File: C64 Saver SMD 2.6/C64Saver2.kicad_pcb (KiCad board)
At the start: 2 copper layers, 43.9 x 28.8 mm, 26 parts, among them J1 Conn_01x04, J2 Conn_01x08, J4 Conn_01x08, J5 Conn_01x04, J6 Conn_01x04, Q1 2N7002, Q2 IRFR5305, U1 TL431DBZ

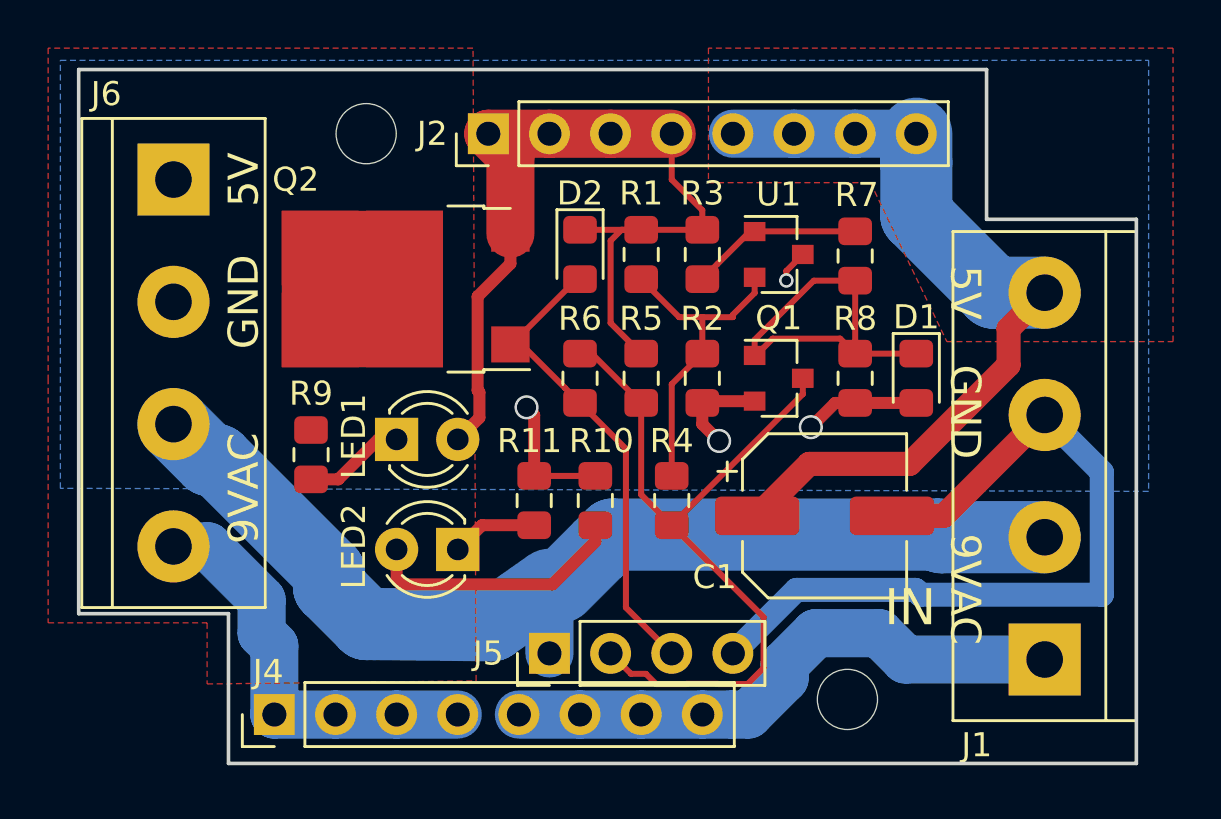
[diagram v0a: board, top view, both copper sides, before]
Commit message: SMD version 2.6 layout and schematics. Both THT and SMD are now on same version. should have same references.
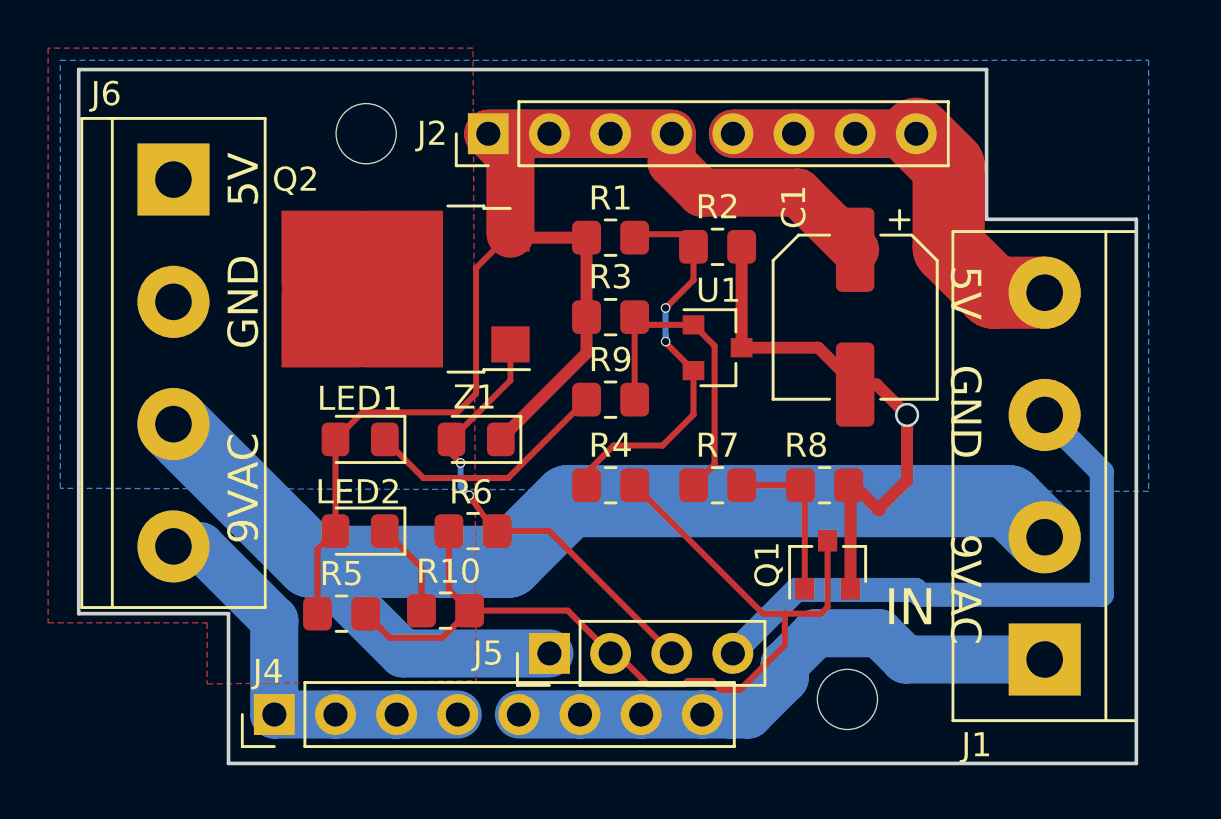
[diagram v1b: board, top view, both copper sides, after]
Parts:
- removed D1, D2: BZY55B6V8, Diode_SMD:D_0805_2012Metric_Pad1.15x1.40mm_HandSolder
- removed R11: 3k3, Resistor_SMD:R_0805_2012Metric_Pad1.15x1.40mm_HandSolder
- added Z1: BZY55B6V8, Diode_SMD:D_0805_2012Metric_Pad1.15x1.40mm_HandSolder, F.Cu at (157.0, 99.1)
- LED1, LED2: footprint LED_THT:LED_D3.0mm -> LED_SMD:LED_0805_2012Metric_Pad1.15x1.40mm_HandSolder
- Q1: value 2N7002 -> BC847
- R1, R2, R3, R4, R5, R6, R7: footprint Resistor_SMD:R_0805_2012Metric_Pad1.15x1.40mm_HandSolder -> Resistor_SMD:R_0805_2012Metric_Pad1.20x1.40mm_HandSolder
- R10, R9: value 3k3 -> 1k; footprint Resistor_SMD:R_0805_2012Metric_Pad1.15x1.40mm_HandSolder -> Resistor_SMD:R_0805_2012Metric_Pad1.20x1.40mm_HandSolder
- R8: value 82k -> 10k; footprint Resistor_SMD:R_0805_2012Metric_Pad1.15x1.40mm_HandSolder -> Resistor_SMD:R_0805_2012Metric_Pad1.20x1.40mm_HandSolder
- moved R5 15.8 mm to (151.4, 106.3), turned to 0 degrees
- moved R9 12.7 mm to (162.6, 97.4), turned to 0 degrees
- moved R7 11.1 mm to (167.0, 101.0), turned to 0 degrees
- moved C1 8.35 mm to (172.7, 94.0), turned to -90 degrees
- moved Q1 8.01 mm to (171.6, 104.3), turned to 90 degrees
- moved R6 7.75 mm to (156.8, 102.9), turned to 180 degrees
- moved R10 7.72 mm to (155.7, 106.2), turned to 180 degrees
- moved R2 5.50 mm to (167.0, 91.1), turned to 0 degrees
- moved U1 4.63 mm to (167.0, 95.2)
- moved R8 4.62 mm to (171.4, 101.0), turned to 0 degrees
- moved R3 4.61 mm to (162.6, 94.0), turned to 0 degrees
- moved LED2 4.13 mm to (152.2, 102.9)
- moved R4 2.62 mm to (162.6, 101.0), turned to 0 degrees
- moved LED1 1.51 mm to (152.2, 99.1), turned to 180 degrees
- moved R1 1.45 mm to (162.6, 90.7), turned to 0 degrees
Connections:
- C1 pad 1: /VCC1+ -> /VCC1-
- LED1 pad 1: Net-(LED1-Pad1) -> Net-(LED1-K)
- LED2 pad 1: Net-(LED2-Pad1) -> Net-(LED2-K)
- LED2 pad 2: /5V_SAFE -> /VCC1-
- R10 pad 1: GND -> OVERVOLTAGE
- R10 pad 2: /5V_SAFE -> Net-(LED2-K)
- R3 pad 2: Net-(R3-Pad2) -> Net-(U1-K)
- R7 pad 1: Net-(R3-Pad2) -> Net-(U1-K)
- R9 pad 1: /5V_SAFE -> Net-(LED1-K)
- R9 pad 2: Net-(LED1-Pad1) -> Net-(U1-K)
- U1 pad 1: Net-(R3-Pad2) -> Net-(U1-K)
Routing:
- net /VCC1-: track 38.3 -> 64.6 mm
- net Net-(U1-K): track 0.00 -> 13.8 mm
- net /5V_SAFE: track 11.0 -> 0.00 mm
- net Net-(LED1-K): track 0.00 -> 10.4 mm
- net /NGATE: track 16.1 -> 6.82 mm
- net /VCC1+: track 34.3 -> 25.3 mm
- net /9VAC2: track 44.9 -> 53.3 mm
- net Net-(R3-Pad2): track 7.17 -> 0.00 mm
- net OVERVOLTAGE: track 32.0 -> 38.6 mm
- net Net-(LED1-Pad1): track 4.24 -> 0.00 mm
- net Net-(LED2-K): track 0.00 -> 3.93 mm
- net Net-(LED2-Pad1): track 3.59 -> 0.00 mm
- net /SENSE: track 13.6 -> 16.9 mm, vias 0 -> 2
- net GND: track 48.8 -> 47.6 mm, vias 4 -> 1
- net PGATE: track 19.9 -> 19.4 mm, vias 0 -> 2
- removed copper zone on F.Cu, net /VCC1+
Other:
- net class Default removed
- net class POWER removed
- board text added: "C64 Saver 2.6 SMD VERSION BWACK 2020"
- board text removed: "2.4"
- board text removed: "2018-09-23"
- board text removed: "C64 Saver"
- board text removed: "C64 Saver 2.5 BWACK 2020"

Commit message: layout for tht 2.6. added connector for leds as alternative to smd leds
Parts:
- added J7: Conn_01x02_Socket, Connector_PinHeader_2.54mm:PinHeader_1x02_P2.54mm_Vertical, F.Cu at (151.3, 98.4)
- added J8: Conn_01x02_Socket, Connector_PinHeader_2.54mm:PinHeader_1x02_P2.54mm_Vertical, F.Cu at (151.3, 102.1)
- moved R6 10.3 mm to (167.0, 104.4)
- moved R10 7.08 mm to (162.6, 104.4)
- moved R5 6.87 mm to (158.0, 104.4)
- moved LED1 6.04 mm to (151.3, 105.0)
- moved LED2 4.53 mm to (151.3, 107.3)
- moved Z1 1.02 mm to (158.0, 99.1)
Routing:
- net /VCC1-: track 64.6 -> 76.0 mm
- net Net-(J8-Pin_2): track 3.93 -> 14.5 mm
- net /9VAC2: track 53.3 -> 43.2 mm
- net Net-(J7-Pin_2): track 10.4 -> 17.8 mm, vias 0 -> 2
- net PGATE: track 19.4 -> 26.1 mm
- net GND: track 47.6 -> 51.7 mm, vias 1 -> 0
- net OVERVOLTAGE: track 38.6 -> 36.6 mm

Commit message: Preparing for Saver 2.6, moving 2.5 and 2.4 to oldfiles folder
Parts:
- moved J1 0.25 mm to (180.3, 108.2)
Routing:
- net /SENSE: track 16.9 -> 20.5 mm
- net Net-(J7-Pin_2): track 17.8 -> 19.8 mm
- net Net-(U1-K): track 13.8 -> 15.4 mm
- net /9VAC2: track 43.2 -> 44.5 mm
- net PGATE: track 26.1 -> 26.8 mm
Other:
- board text added: "C64 Saver 2.6 SMD VERSION BWACK 2023"
- board text removed: "C64 Saver 2.6 SMD VERSION BWACK 2020"
